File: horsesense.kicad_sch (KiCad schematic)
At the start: 0 parts

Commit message: Routage complet
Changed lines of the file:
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@@
 	(paper "A4")
 	(sheet
-		(at 81.28 35.56)
-		(size 43.18 22.86)
+		(at 101.6 93.98)
+		(size 95.25 8.89)
 		(exclude_from_sim no)
 		(in_bom yes)
@@
 		)
 		(property "Sheetname" "MCU"
-			(at 81.28 34.8484 0)
+			(at 101.6 93.2684 0)
 			(effects
 				(font
@@
 		)
 		(property "Sheetfile" "mcu.kicad_sch"
-			(at 81.28 59.0046 0)
+			(at 101.6 103.4546 0)
 			(effects
 				(font
@@
 	)
 	(sheet
-		(at 87.63 147.32)
-		(size 45.72 19.05)
+		(at 72.39 80.01)
+		(size 26.67 22.86)
 		(exclude_from_sim no)
 		(in_bom yes)
@@
 		)
 		(property "Sheetname" "power"
-			(at 87.63 146.6084 0)
+			(at 72.39 79.2984 0)
 			(effects
 				(font
@@
 		)
 		(property "Sheetfile" "power.kicad_sch"
-			(at 87.63 166.9546 0)
+			(at 72.39 103.4546 0)
 			(effects
 				(font
@@
 	)
 	(sheet
-		(at 87.63 110.49)
-		(size 45.72 20.32)
+		(at 151.13 80.01)
+		(size 45.72 8.89)
 		(exclude_from_sim no)
 		(in_bom yes)
@@
 		)
 		(property "Sheetname" "GPS"
-			(at 87.63 109.7784 0)
+			(at 151.13 79.2984 0)
 			(effects
 				(font
@@
 		)
 		(property "Sheetfile" "gps.kicad_sch"
-			(at 87.63 131.3946 0)
+			(at 151.13 89.4846 0)
 			(effects
 				(font
@@
 	)
 	(sheet
-		(at 85.09 73.66)
-		(size 46.99 20.32)
+		(at 101.6 80.01)
+		(size 46.99 8.89)
 		(exclude_from_sim no)
 		(in_bom yes)
@@
 		)
 		(property "Sheetname" "capteur"
-			(at 85.09 72.9484 0)
+			(at 101.6 79.2984 0)
 			(effects
 				(font
@@
 		)
 		(property "Sheetfile" "capteur.kicad_sch"
-			(at 85.09 94.5646 0)
+			(at 101.6 89.4846 0)
 			(effects
 				(font

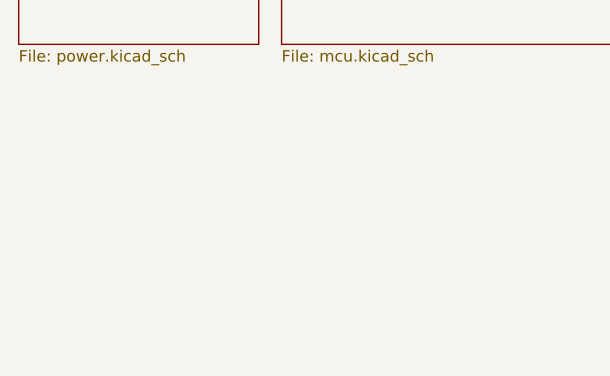
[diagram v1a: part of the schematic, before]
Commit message: Add mire and sizing marks
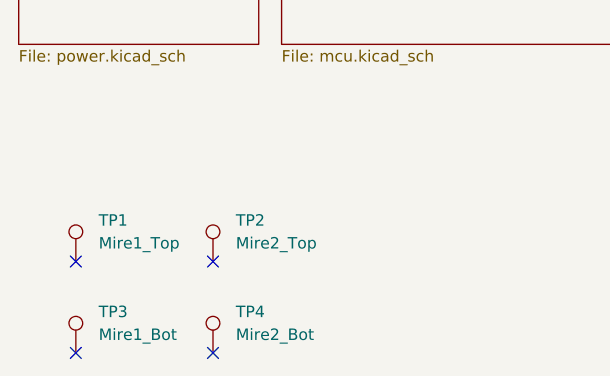
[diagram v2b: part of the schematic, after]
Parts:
- added TP1: Mire1_Top, TestPoint:TestPoint_Pad_D1.0mm, symbol Connector:TestPoint
- added TP2: Mire2_Top, TestPoint:TestPoint_Pad_D1.0mm, symbol Connector:TestPoint
- added TP3: Mire1_Bot, TestPoint:TestPoint_Pad_D1.0mm, symbol Connector:TestPoint
- added TP4: Mire2_Bot, TestPoint:TestPoint_Pad_D1.0mm, symbol Connector:TestPoint
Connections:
- no-connect marks 0 -> 4

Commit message: Ass logo
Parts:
- added SYM1: https://github.com/Philippe12/HorseSense, Symbol:OSHW-Symbol_13.4x12mm_SilkScreen, symbol Graphic:Logo_Open_Hardware_Large
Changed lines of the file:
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@@
+		)
+	)
+	(symbol
+		(lib_id "Graphic:Logo_Open_Hardware_Large")
+		(at 134.62 129.54 0)
+		(unit 1)
+		(exclude_from_sim no)
+		(in_bom no)
+		(on_board yes)
+		(dnp no)
+		(fields_autoplaced yes)
+		(property "Reference" "SYM1"
+			(at 134.62 116.84 0)
+			(effects
+				(font
+					(size 1.27 1.27)
+				)
+				(hide yes)
+			)
+		)
+		(property "Value" "https://github.com/Philippe12/HorseSense"
+			(at 134.62 139.7 0)
+			(effects
+				(font
+					(size 1.27 1.27)
+				)
+			)
+		)
+		(property "Footprint" "Symbol:OSHW-Symbol_13.4x12mm_SilkScreen"
+			(at 134.62 129.54 0)
+			(effects
+				(font
+					(size 1.27 1.27)
+				)
+				(hide yes)
+			)
+		)
+		(property "Datasheet" "~"
+			(at 134.62 129.54 0)
+			(effects
+				(font
+					(size 1.27 1.27)
+				)
+				(hide yes)
+			)
+		)
+		(property "Description" "Open Hardware logo, large"
+			(at 134.62 129.54 0)
+			(effects
+				(font
+					(size 1.27 1.27)
+				)
+				(hide yes)
+			)
+		)
+		(property "Sim.Enable" "0"
+			(at 134.62 129.54 0)
+			(effects
+				(font
+					(size 1.27 1.27)
+				)
+				(hide yes)
+			)
+		)
+		(instances
+			(project ""
+				(path "/f18e9cf6-8519-4493-9888-bebeac60f18c"
+					(reference "SYM1")
+					(unit 1)
+				)
+			)
 		)
 	)

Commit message: Add version
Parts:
- SYM1: Version (none) -> V1.0
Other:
- company: (none) -> Philippe12
- title: (none) -> HorseSense
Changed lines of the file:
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@@
 	(generator_version "9.0")
 	(paper "A4")
+	(title_block
+		(title "HorseSense")
+		(date "2025-11-01")
+		(rev "1.0")
+		(company "Philippe12")
+	)
 	(no_connect
 		(at 93.98 137.16)
@@
 		(on_board yes)
 		(dnp no)
-		(fields_autoplaced yes)
 		(property "Reference" "SYM1"
 			(at 134.62 116.84 0)
@@
 			)
 		)
+		(property "Version" "V1.0"
+			(at 134.62 142.494 0)
+			(effects
+				(font
+					(size 1.27 1.27)
+				)
+			)
+		)
